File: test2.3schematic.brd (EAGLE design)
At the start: 16.4 x 22.3 mm, 24 parts, among them IC1 NCS21911SN2T1G, IC2 FXLN8371QR1, IC3 MAX25210ATAB9_V+, IC4 NCS21911SN2T1G, IC5 NCS21911SN2T1G

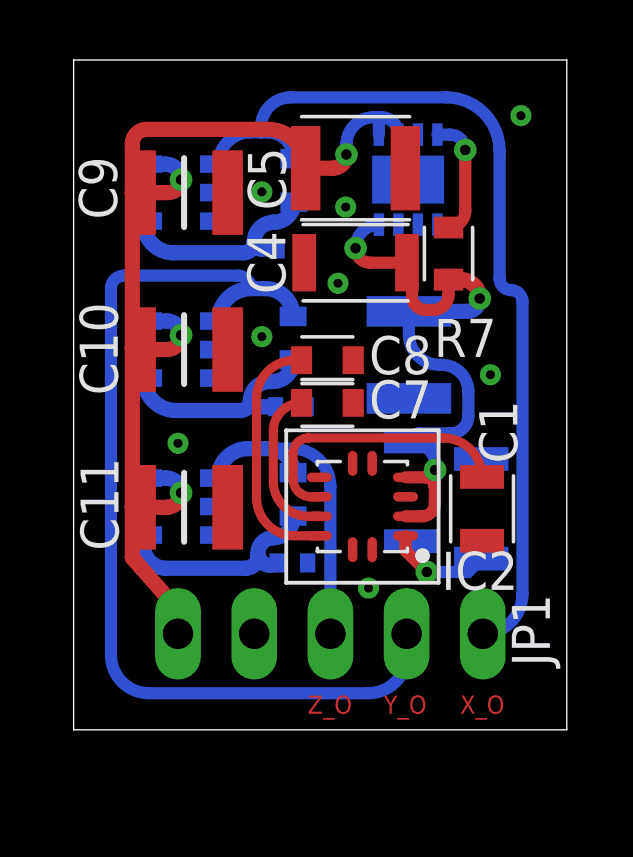
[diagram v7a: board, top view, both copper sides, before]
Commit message: Just 2 airwires left to connect, waiting for Forrest Review
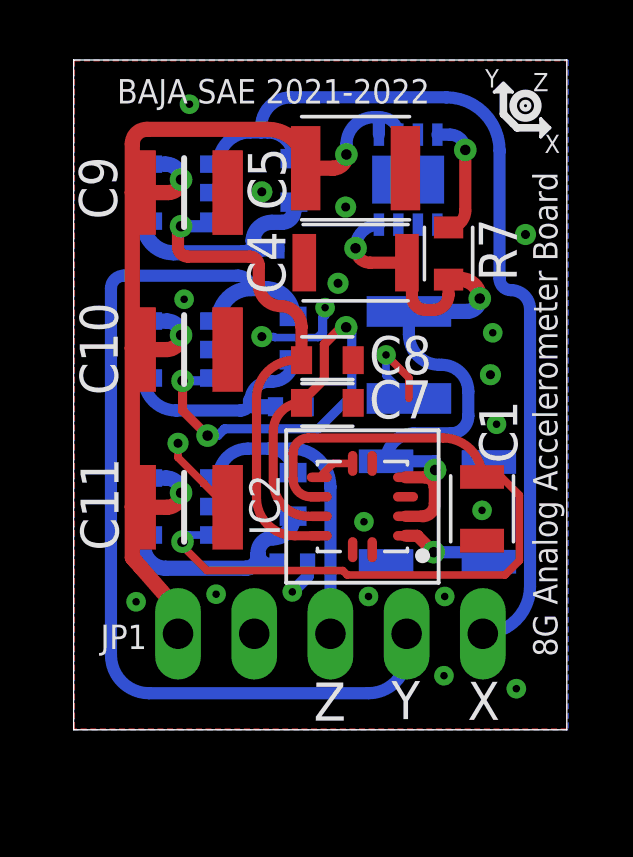
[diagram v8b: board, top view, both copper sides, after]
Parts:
- moved C3 1.07 mm to (9.73, 6.63)
- moved C6 0.27 mm to (13.2, 6.60)
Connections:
- new net X_OUT_F: IC1.4, R2.1, R6.2
- new net Y_OUT_F: IC4.4, R3.1, R5.2
- new net Z_OUT_F: IC5.4, R1.2, R4.1
- net X_OUT: no longer IC1.4, R2.1, R6.2
- net Y_OUT: no longer IC4.4, R3.1, R5.2
- net Z_OUT: no longer IC5.4, R1.2, R4.1
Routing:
- net Z_AXIS: track 9.03 -> 26.0 mm, vias 0 -> 1
- net Y_AXIS: track 5.02 -> 19.4 mm, vias 0 -> 3
- net GND: track 0.00 -> 12.1 mm, vias 8 -> 22
- net X_AXIS: track 7.96 -> 16.7 mm, vias 0 -> 1
- net X_OUT_F: track 0.00 -> 7.29 mm
- net Z_OUT: track 17.8 -> 10.7 mm
- net Z_OUT_F: track 0.00 -> 7.13 mm
- net Y_OUT_F: track 0.00 -> 7.07 mm
- net Y_OUT: track 39.2 -> 32.2 mm
- net X_OUT: track 36.7 -> 29.8 mm
- net V_3.3V: track 21.5 -> 23.2 mm
- added copper zone on layer 1, net GND
- added copper zone on layer 16, net GND
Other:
- board text added: "8G Analog Accelerometer Board"
- board text added: "BAJA SAE 2021-2022"
- board text added: "Kevin Foyet"
- board text added: "X"
- board text added: "Y"
- board text added: "Z"
- board text removed: "X_O"
- board text removed: "Y_O"
- board text removed: "Z_O"
